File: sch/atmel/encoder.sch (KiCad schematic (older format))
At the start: 58 parts, among them J1 CONN_01X02, J2 CAN, J3 ICSP, Q1 MMBT2222A, U1 ATMEGA328P-PU, U2 LM7805CV, U3 DS1307, U4 PSW-8,5R, U5 PESD1CAN, U6 MPC2551, U7 MCP2515-E/SO, U8 MAX485CSA, Y1 16MHz, Y2 32.768KHz, Y3 16MHz

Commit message: Signed-off-by: cuki2 <mauricio@krebs.com.br>
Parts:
- added D4: ENCODER, w_smd_leds:Led_0805, symbol LED_AK
- added D5: CAN, w_smd_leds:Led_0805, symbol LED_AK
- added R11, R6: 1k, w_smd_resistors:r_0805, symbol R
- RLY1: renamed from RLY?; value RELAY_9001 -> SH1NAC-5V; footprint (none) -> w_relay:relay_9001; Equitronic (none) -> 1997; MNP (none) -> SH1NAC-5V
- U6: footprint (none) -> w_smd_dil:so-8; Equitronic (none) -> 4324; MNP (none) -> MCP2551E/SN
- gave numbers to parts that had none: 5
- renumbered C12 to C11, C11 to C12, C14 to C13, C13 to C14, C16 to C15, C17 to C16, C15 to C17, D2 to D3, D3 to D6, D4 to D7, J2 to J4, Q1 to Q2, R7 to R10, R9 to R12, R10 to R13, R11 to R14, R12 to R15, R8 to R16, R13 to R17, R14 to R18, R15 to R19, R3 to R5, R4 to R7, R5 to R8, R6 to R9
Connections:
- net +5V: now also D5.2 (K)
- net CAN_SCK: now also R11.2
- net GND: now also D4.2 (K)
- net at J2.4 (P4), RLY1.1: now also R6.2
- new net: D4.1 (A), R6.1
- new net: D5.1 (A), R11.1
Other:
- moved on the sheet: BT1, C1, C10, C2, C3, C4, C6, D2, J2, Q1, R1, R2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

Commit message: Signed-off-by: cuki2 <mauricio@krebs.com.br>
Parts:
- added DS1: LCD-016N002L, w_indicators:lcd_16x2, symbol LCD-016N002L
- added R6: 560R, w_smd_resistors:r_0805, symbol R
- added RV1: POT, w_smd_resistors:trim_murata_pva2a, symbol POT
- C3: renamed from C2; footprint w_capacitors:CP_4x5mm -> w_capacitors:CP_5x11mm
- J1: value CONN_01X02 -> GND-24V
- U1: footprint w_pth_circuits:dil_28-300_socket -> w_smd_lqfp:lqfp32
- renumbered C9 to C10, C4 to C2, C3 to C4, C6 to C5, C5 to C6, C10 to C8, C8 to C9, R9 to R10, R10 to R11, R11 to R12, R12 to R13, R13 to R14, R14 to R15, R15 to R16, R16 to R17, R17 to R18, R18 to R19, R19 to R20, R6 to R7, R7 to R8, R8 to R9, U3 to U2, U2 to U3
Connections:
- net +5V: now also DS1.15 (LED+), DS1.2 (VDD), RV1.3
- net +BATT: now also U1.26 ((PCINT11/ADC3)PC3); no longer U1.11 ((PCINT23/AIN1)PD7)
- net CAN_H: now also J4.2 (P2); no longer J4.1 (P1)
- net CAN_INT: now also U1.32 ((PCINT18/INT0)PD2); no longer U1.12 ((PCINT0/CLKO/ICP1)PB0)
- net CAN_L: now also J4.1 (P1); no longer J4.2 (P2)
- net GND: now also DS1.1 (VSS), DS1.5 (R/W), R6.2, RV1.1
- net LCD_D6: now reaches U1.10 ((PCINT22/OC0A/AIN0)PD6)
- net LCD_D6: now also DS1.13 (D6)
- net LCD_D4: now reaches U1.2 ((PCINT20/XCK/T0)PD4)
- net LCD_D4: now also DS1.11 (D4)
- net LCD_RS: now reaches U1.24 ((PCINT9/ADC1)PC1)
- net LCD_RS: now also DS1.4 (RS)
- net LCD_EN: now reaches U1.25 ((PCINT10/ADC2)PC2)
- net LCD_EN: now also DS1.6 (E)
- net LCD_D5: now reaches U1.9 ((PCINT21/OC0B/T1)PD5)
- net LCD_D5: now also DS1.12 (D5)
- new net: DS1.16 (LED-), R6.1
- new net: DS1.3 (VO), RV1.2
- new net LCD_D7: DS1.14 (D7), U1.11 ((PCINT23/AIN1)PD7)
- no-connect marks 18 -> 16

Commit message: lcd e heart_beat
Signed-off-by: cuki2 <mauricio@krebs.com.br>
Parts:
- added D8: RUN, w_smd_leds:Led_0805, symbol LED_AK
- added R21: 1k, w_smd_resistors:r_0805, symbol R
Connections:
- net CAN_RS: now also U1.12 ((PCINT0/CLKO/ICP1)PB0); no longer U1.13 ((PCINT1/OC1A)PB1)
- net GND: now also D8.2 (K)
- new net: D8.1 (A), R21.1
- new net HEART_BEAT: R21.2, U1.13 ((PCINT1/OC1A)PB1)
- no-connect marks 16 -> 15
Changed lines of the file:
@@
 Text Label 4250 2450 2    60   ~ 0
 CAN_CS
-Text Label 4250 2350 2    60   ~ 0
+Text Label 4250 2250 2    60   ~ 0
 CAN_RS
 Text Label 4250 4050 2    60   ~ 0
@@
 	4250 4050 3600 4050
 NoConn ~ 3600 4150
-NoConn ~ 3600 2250
 Wire Wire Line
 	4250 3200 3600 3200
@@
 Wire Wire Line
 	4400 3400 4400 3350
+Wire Wire Line
+	3600 2250 4250 2250
+Text Label 4250 2350 2    60   ~ 0
+HEART_BEAT
+$Comp
+L R R21
+U 1 1 595BF765
+P 5700 2250
+F 0 "R21" V 5780 2250 50  0000 C CNN
+F 1 "1k" V 5700 2250 50  0000 C CNN
+F 2 "w_smd_resistors:r_0805" V 5630 2250 50  0001 C CNN
+F 3 "http://www.mouser.com/ds/2/315/AOA0000C237-1100991.pdf" H 5700 2250 50  0001 C CNN
+F 4 "ERA-6AEB102V" V 5700 2250 60  0001 C CNN "MNP"
+F 5 "2527" V 5700 2250 60  0001 C CNN "Equitronic"
+	1    5700 2250
+	0    1    1    0
+$EndComp
+Wire Wire Line
+	6000 2450 6000 2250
+Wire Wire Line
+	6000 2250 5850 2250
+$Comp
+L GND #PWR067
+U 1 1 595BF76D
+P 6000 2900
+F 0 "#PWR067" H 6000 2650 50  0001 C CNN
+F 1 "GND" H 6000 2750 50  0000 C CNN
+F 2 "" H 6000 2900 50  0001 C CNN
+F 3 "" H 6000 2900 50  0001 C CNN
+	1    6000 2900
+	1    0    0    -1
+$EndComp
+Wire Wire Line
+	6000 2900 6000 2750
+Wire Wire Line
+	5550 2250 5000 2250
+Text Label 5000 2250 0    60   ~ 0
+HEART_BEAT
+$Comp
+L LED_AK D8
+U 1 1 595C10CC
+P 6000 2600
+F 0 "D8" H 6000 2700 50  0000 C CNN
+F 1 "RUN" H 6000 2500 50  0000 C CNN
+F 2 "w_smd_leds:Led_0805" H 6000 2600 50  0001 C CNN
+F 3 "http://www.mouser.com/ds/2/678/V02-0977EN0-909004.pdf" H 6000 2600 50  0001 C CNN
+F 4 "HSMR-C170-R0000" H 6000 2600 60  0001 C CNN "MNP"
+F 5 "452" H 6000 2600 60  0001 C CNN "Equitronic"
+	1    6000 2600
+	0    -1   -1   0
+$EndComp
 $EndSCHEMATC

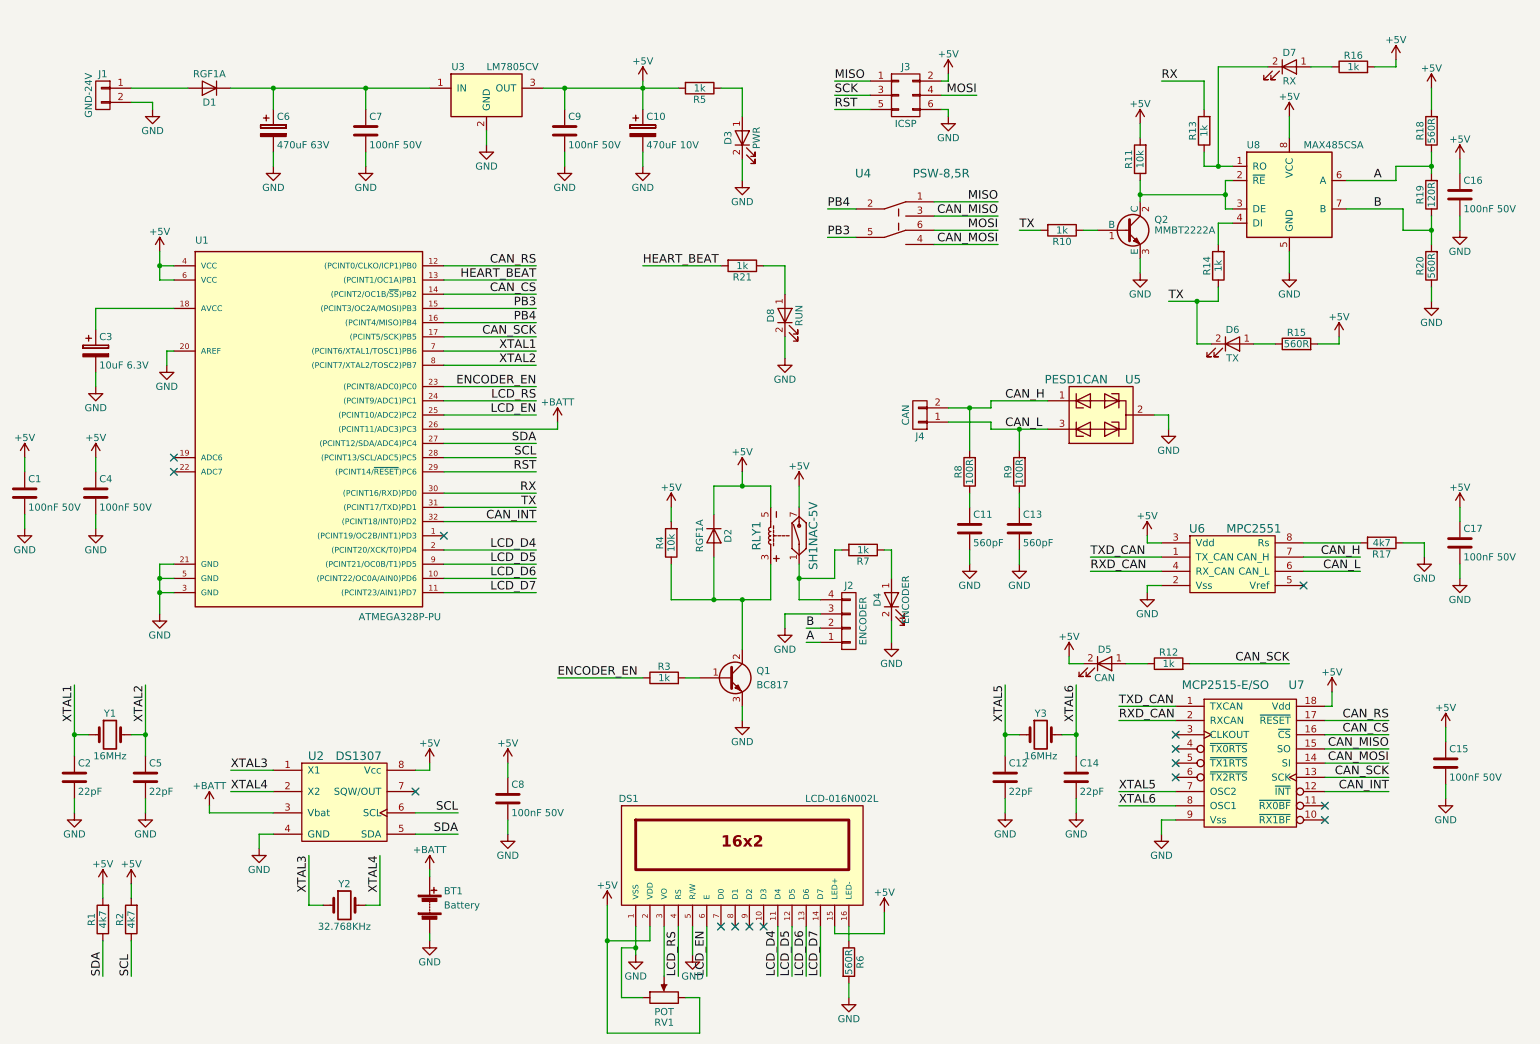
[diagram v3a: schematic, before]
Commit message: regulador tensao d2pak
Signed-off-by: cuki2 <mauricio@krebs.com.br>
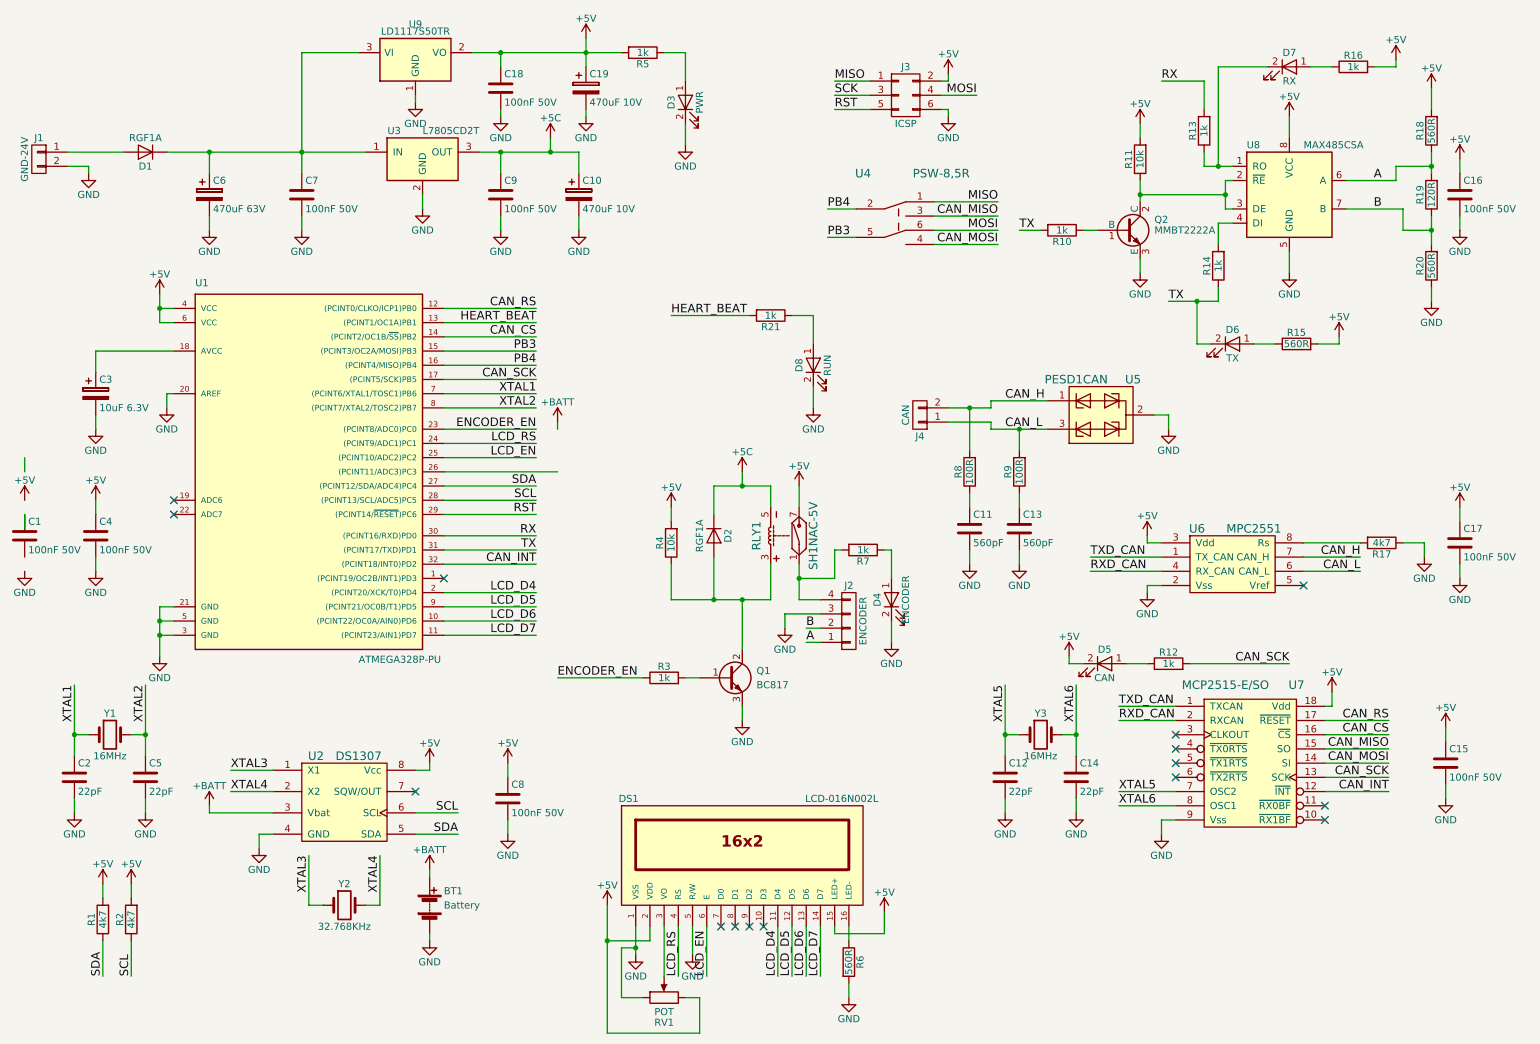
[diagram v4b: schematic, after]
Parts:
- added C18: 100nF 50V, w_smd_cap:c_0805, symbol C
- added C19: 470uF 10V, w_capacitors:CP_8x11.5mm, symbol CP
- added U9: LD1117S50TR, w_smd_trans:sot223, symbol LD1117S50TR
- Q1: Equitronic - -> 6888
- U3: value LM7805CV -> L7805CD2T; footprint w_to:to220_5772 -> w_smd_trans:d2-pak; Equitronic 16316 -> 12060; MNP LM7805CV -> L7805CD2T
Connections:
- net +5V: now also C18.1, C19.1, U9.2 (VO); no longer C1.1, C10.1, C9.1, D2.2 (K), RLY1.5, U3.3 (OUT)
- net +BATT: no longer U1.26 ((PCINT11/ADC3)PC3)
- net GND: now also C18.2, C19.2, U9.1 (GND); no longer C1.2
- net at C6.1, C7.1, D1.2 (K)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: now also U9.3 (VI)
- new net +5C: C10.1, C9.1, D2.2 (K), RLY1.5, U3.3 (OUT)
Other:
- moved on the sheet: C1, C10, C3, C4, C6, C7, C9, D1, D3, D8, J1, R21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

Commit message: Signed-off-by: cuki2 <mauricio@krebs.com.br>
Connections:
- net +5V: now also C1.1
- net +BATT: now also U1.26 ((PCINT11/ADC3)PC3)
- net GND: now also C1.2
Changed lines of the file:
@@
 F 1 "L7805CD2T" H 3450 1700 50  0000 L CNN
 F 2 "w_smd_trans:d2-pak" H 3450 1600 50  0001 C CIN
-F 3 "https://www.sparkfun.com/datasheets/Components/LM7805.pdf" H 3450 1500 50  0001 C CNN
+F 3 "http://www.farnell.com/datasheets/2307057.pdf?_ga=2.257182158.436367794.1499186680-1980578707.1499186680" H 3450 1500 50  0001 C CNN
 F 4 "L7805CD2T" H 3450 1500 60  0001 C CNN "MNP"
 F 5 "12060" H 3450 1500 60  0001 C CNN "Equitronic"
@@
 	1    0    0    -1
 $EndComp
-Wire Wire Line
-	650  4100 650  4000
 $Comp
 L +5V #PWR039
@@
 	1    0    0    -1
 $EndComp
-Wire Wire Line
-	650  3600 650  3700
 $Comp
 L MCP2515-I/P U7
@@
 $EndComp
 Wire Wire Line
-	3600 3700 4400 3700
-Wire Wire Line
-	4400 3400 4400 3350
+	4400 3700 3600 3700
+Wire Wire Line
+	4400 3350 4400 3700
 Wire Wire Line
 	3600 2550 4250 2550
@@
 	1    0    0    -1
 $EndComp
+Wire Wire Line
+	650  4000 650  3900
+Wire Wire Line
+	650  4300 650  4400
 $EndSCHEMATC

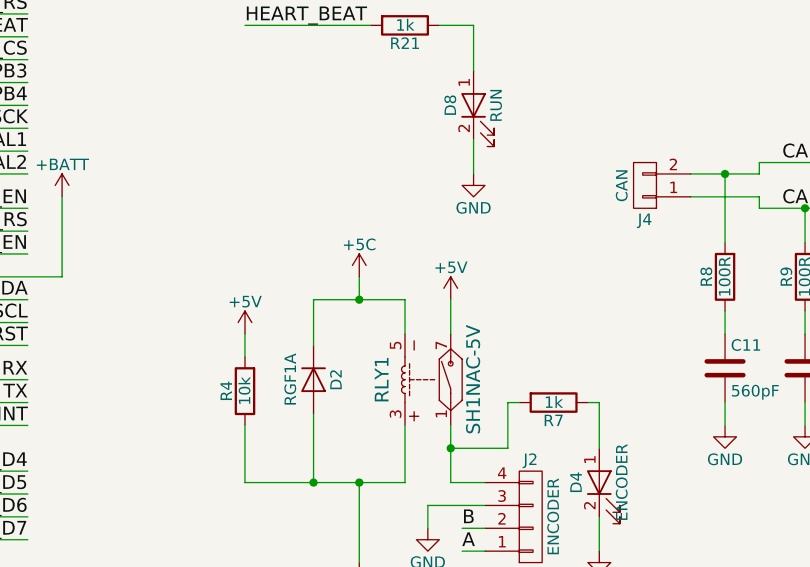
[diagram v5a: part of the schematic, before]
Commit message: correcao rele alimentacao encoder
Signed-off-by: cuki2 <mauricio@krebs.com.br>
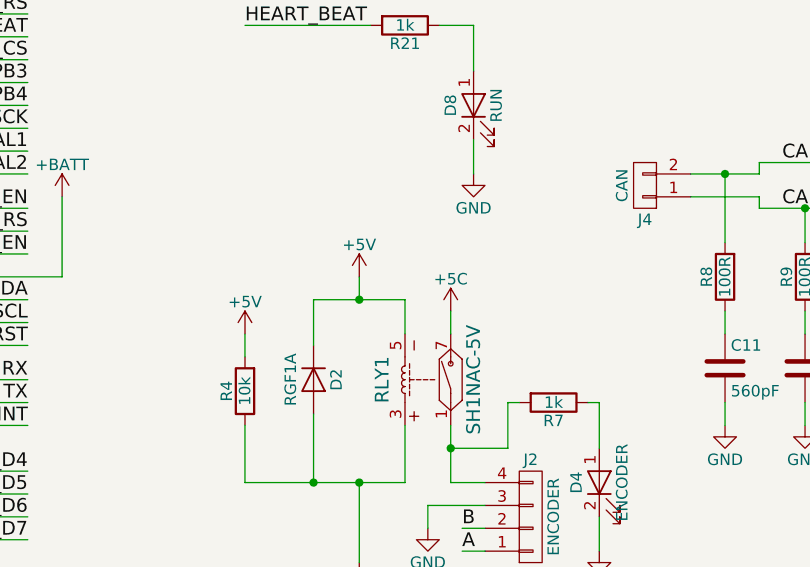
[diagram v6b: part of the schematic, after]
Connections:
- net +5C: now also RLY1.7; no longer D2.2 (K), RLY1.5
- net +5V: now also D2.2 (K), RLY1.5; no longer RLY1.7
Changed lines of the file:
@@
 L +5V #PWR054
 U 1 1 595869AD
-P 6100 3800
-F 0 "#PWR054" H 6100 3650 50  0001 C CNN
-F 1 "+5V" H 6100 3940 50  0000 C CNN
-F 2 "" H 6100 3800 50  0001 C CNN
-F 3 "" H 6100 3800 50  0001 C CNN
-	1    6100 3800
-	1    0    0    -1
-$EndComp
-Wire Wire Line
-	6100 3800 6100 3950
+P 5700 3700
+F 0 "#PWR054" H 5700 3550 50  0001 C CNN
+F 1 "+5V" H 5700 3840 50  0000 C CNN
+F 2 "" H 5700 3700 50  0001 C CNN
+F 3 "" H 5700 3700 50  0001 C CNN
+	1    5700 3700
+	1    0    0    -1
+$EndComp
 Wire Wire Line
 	6100 4600 6250 4600
@@
 	5500 4300 5500 4600
 Connection ~ 5700 4600
-Wire Wire Line
-	5700 3700 5700 3800
 Wire Wire Line
 	5500 3800 5900 3800
@@
 L +5C #PWR071
 U 1 1 595CE4DF
-P 5700 3700
-F 0 "#PWR071" H 5700 3550 50  0001 C CNN
-F 1 "+5C" H 5700 3840 50  0000 C CNN
-F 2 "" H 5700 3700 50  0001 C CNN
-F 3 "" H 5700 3700 50  0001 C CNN
-	1    5700 3700
+P 6100 3850
+F 0 "#PWR071" H 6100 3700 50  0001 C CNN
+F 1 "+5C" H 6100 3990 50  0000 C CNN
+F 2 "" H 6100 3850 50  0001 C CNN
+F 3 "" H 6100 3850 50  0001 C CNN
+	1    6100 3850
 	1    0    0    -1
 $EndComp
@@
 Wire Wire Line
 	650  4300 650  4400
+Wire Wire Line
+	6100 3850 6100 3950
+Wire Wire Line
+	5700 3700 5700 3800
 $EndSCHEMATC
